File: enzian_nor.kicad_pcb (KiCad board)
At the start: 4 copper layers, 75 x 60 mm, 27 parts, among them IC1 L7809ABD2T-TR, J1 ASP-134488-01, U1 MT35XU02GCBA1G12-0AUT

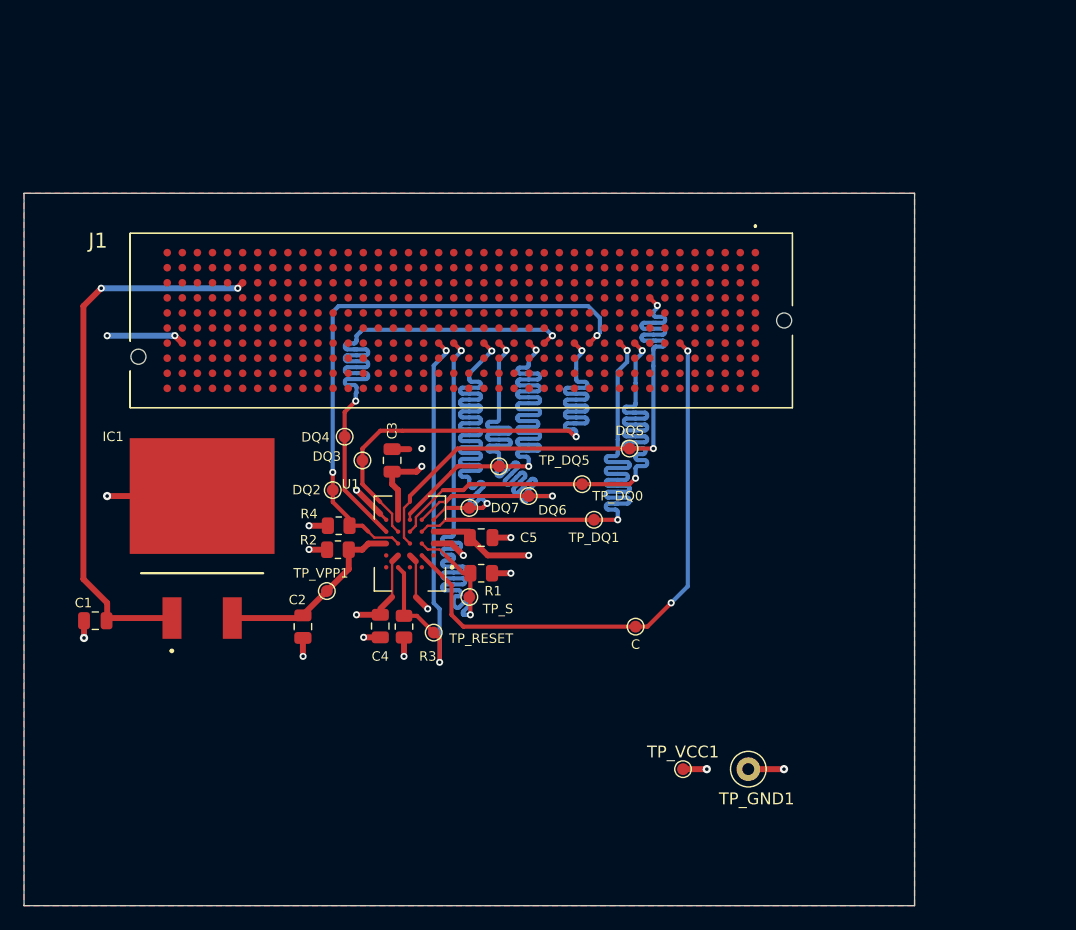
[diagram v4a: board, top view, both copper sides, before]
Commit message: Via stitching for the coplanar ground plane
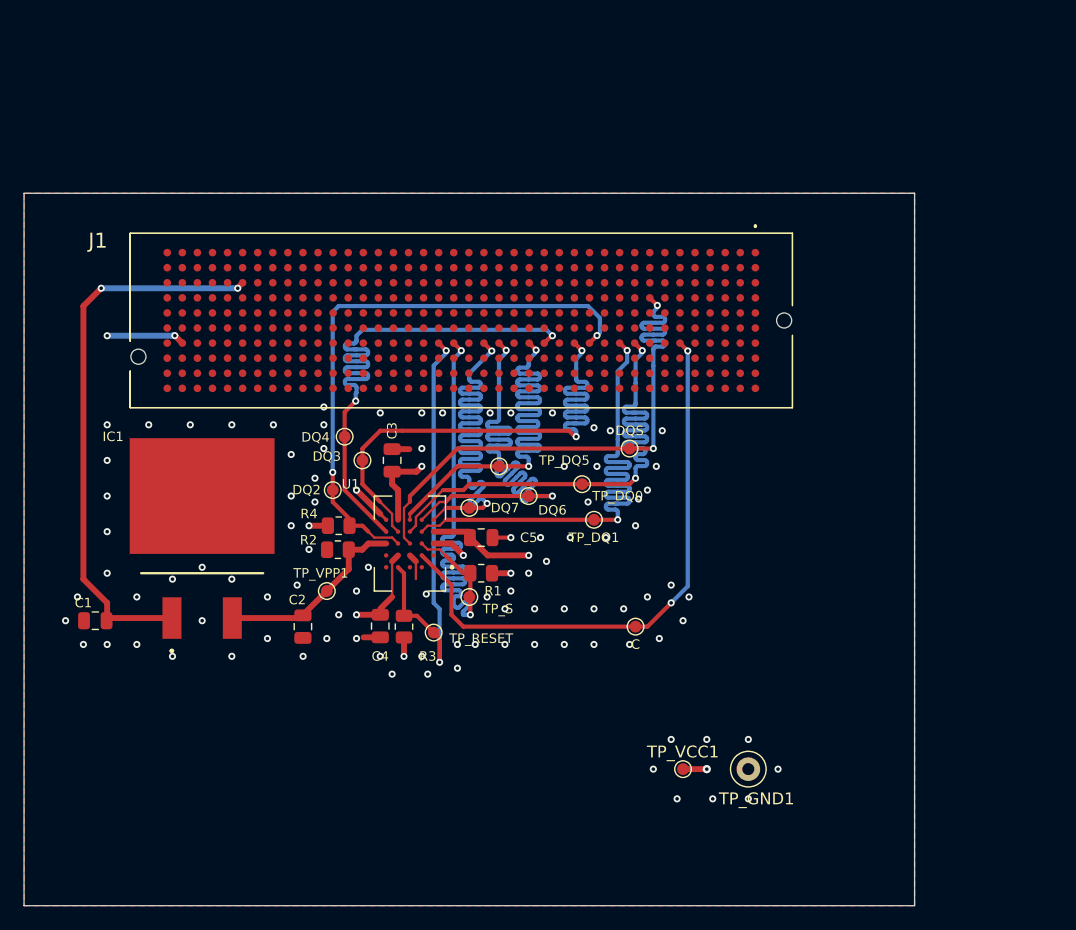
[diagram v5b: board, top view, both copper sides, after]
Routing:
- net GND: track 31.6 -> 13.2 mm, vias 11 -> 97

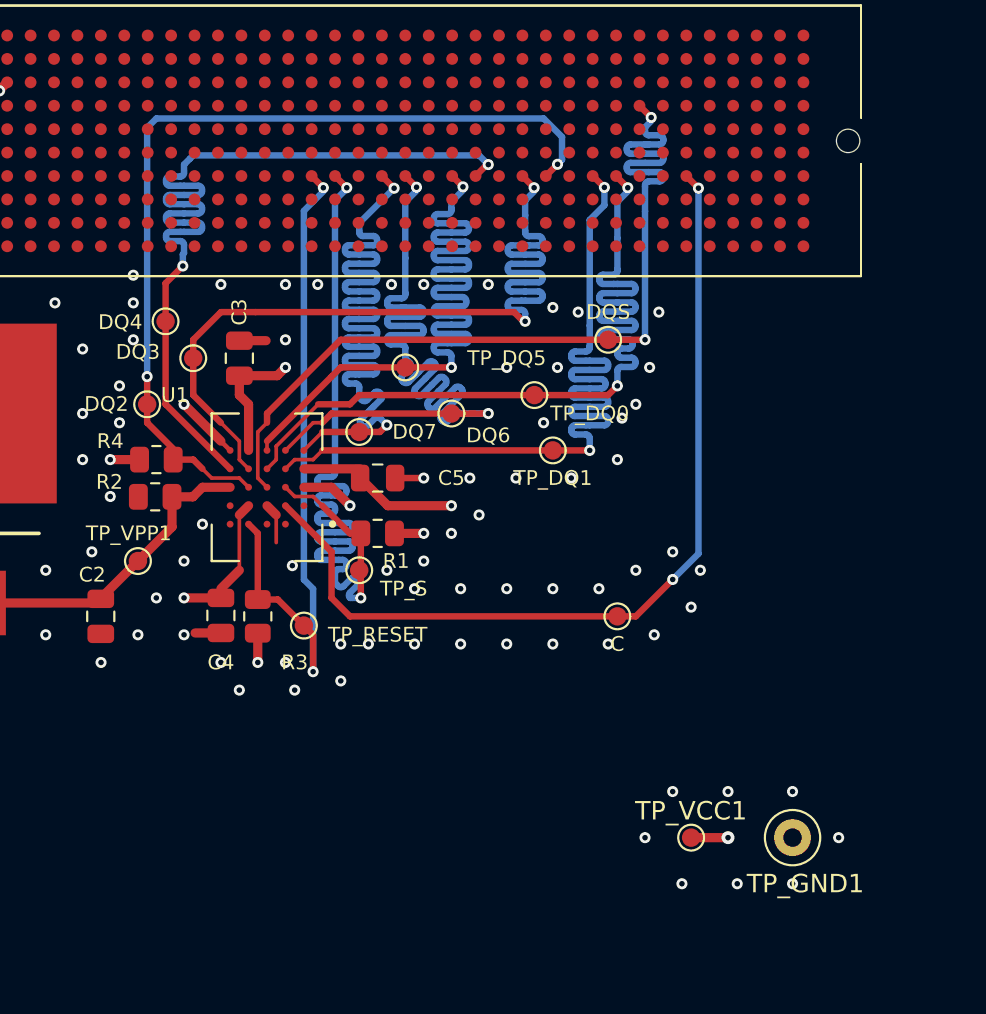
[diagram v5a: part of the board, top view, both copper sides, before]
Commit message: Revised length matching so meanders have 2x trace width between traces
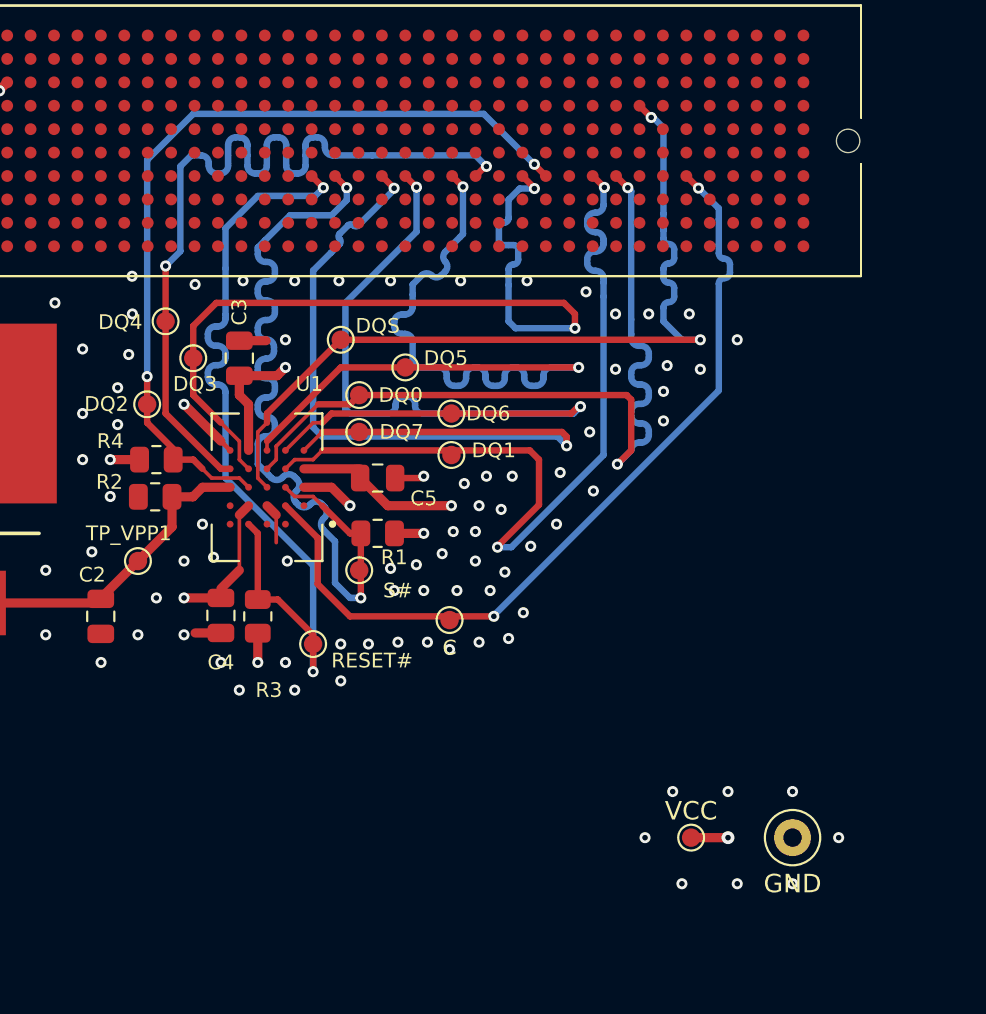
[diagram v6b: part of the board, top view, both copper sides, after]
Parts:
- moved DQS 14.5 mm to (52.5, 101.0)
- moved DQ0 9.50 mm to (53.5, 104.0)
- moved C 9.10 mm to (58.4, 116.2)
- moved DQ1 5.51 mm to (58.5, 107.2)
- moved RESET# 1.12 mm to (51.0, 117.5)
- renumbered TP_DQ0 to DQ0, TP_DQ1 to DQ1, TP_DQ5 to DQ5, TP_GND1 to GND, TP_RESET to RESET#, TP_S to S#, TP_VCC1 to VCC
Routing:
- net /NOR_RESET#: track 37.9 -> 45.5 mm
- net /NOR_S#: track 49.3 -> 45.1 mm
- net /NOR_DQ2: track 49.1 -> 45.6 mm
- net /NOR_DQ3: track 48.8 -> 45.5 mm
- net /NOR_DQ4: track 48.5 -> 45.4 mm
- net /NOR_DQ5: track 48.3 -> 45.3 mm
- net /NOR_C: track 48.5 -> 45.6 mm
- net /NOR_DQ0: track 48.3 -> 45.4 mm
- net /NOR_DQ1: track 48.4 -> 45.5 mm
- net /NOR_DQ6: track 48.3 -> 45.5 mm
- net /NOR_DQS: track 48.4 -> 45.7 mm
- net /NOR_DQ7: track 48.2 -> 45.6 mm
- net GND: vias 97 -> 104

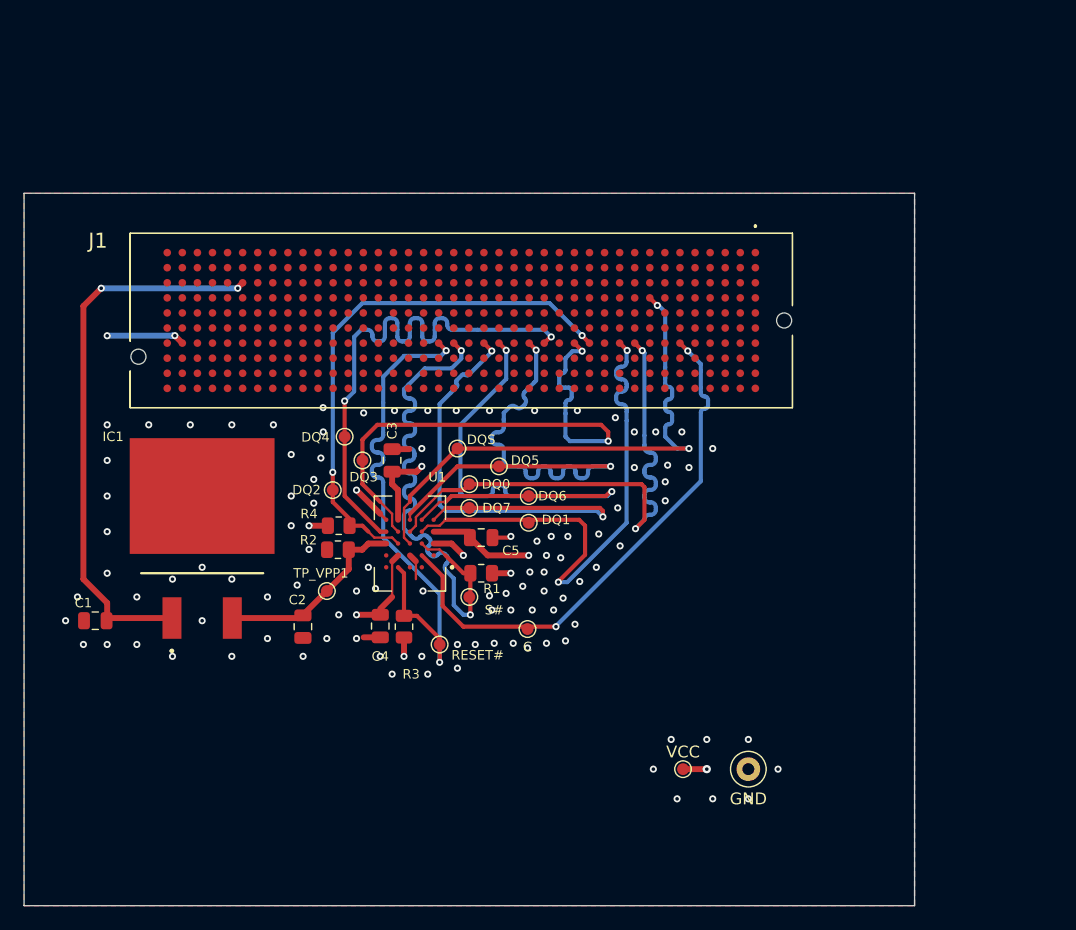
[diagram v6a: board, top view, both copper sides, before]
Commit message: Add version number, mounting holes, and minor changes to via placement
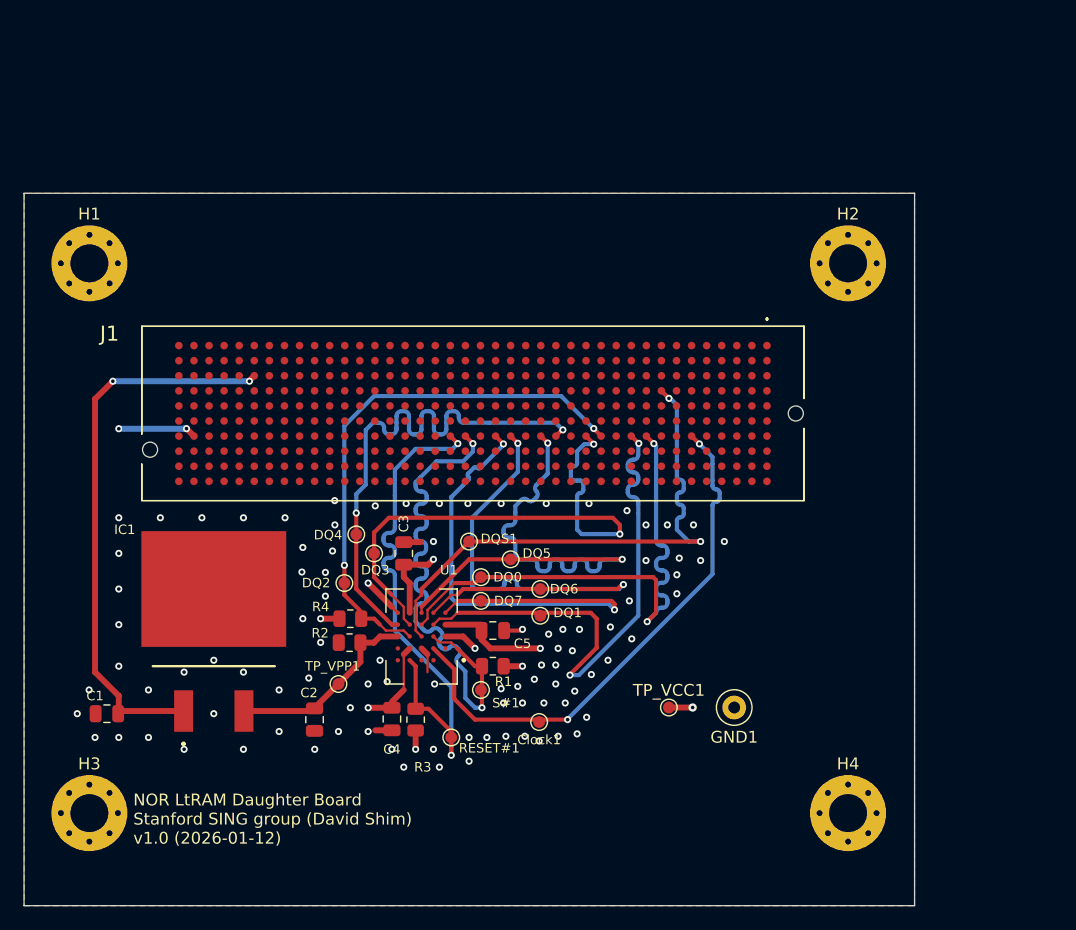
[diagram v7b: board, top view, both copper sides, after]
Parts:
- added H1: MountingHole_Pad, MountingHole:MountingHole_3.2mm_M3_Pad_Via, F.Cu at (21.5, 85.4)
- added H2: MountingHole_Pad, MountingHole:MountingHole_3.2mm_M3_Pad_Via, F.Cu at (85.4, 85.4)
- added H3: MountingHole_Pad, MountingHole:MountingHole_3.2mm_M3_Pad_Via, F.Cu at (21.5, 131.7)
- added H4: MountingHole_Pad, MountingHole:MountingHole_3.2mm_M3_Pad_Via, F.Cu at (85.4, 131.7)
- moved DQ4 8.29 mm to (44.0, 108.2)
- moved C1 7.89 mm to (23.0, 123.3)
- moved C2 7.89 mm to (40.5, 123.8)
- moved C3 7.89 mm to (48.0, 109.8)
- moved C4 7.89 mm to (47.0, 123.8)
- moved C5 7.89 mm to (55.5, 116.3)
- moved Clock1 7.89 mm to (59.4, 124.0)
- moved DQ0 7.89 mm to (54.5, 111.8)
- moved DQ1 7.89 mm to (59.5, 115.1)
- moved DQ2 7.89 mm to (43.0, 112.3)
- moved DQ3 7.89 mm to (45.5, 109.8)
- moved DQ5 7.89 mm to (57.0, 110.3)
- moved DQ6 7.89 mm to (59.5, 112.8)
- moved DQ7 7.89 mm to (54.5, 113.8)
- moved DQS1 7.89 mm to (53.5, 108.8)
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- renumbered C to Clock1, DQS to DQS1, GND to GND1, RESET# to RESET#1, S# to S#1, VCC to TP_VCC1
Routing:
- net GND: vias 104 -> 96
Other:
- board text added: "NOR LtRAM Daughter Board Stanford SING group (David Shim) v1.0 (2026-01-12)"

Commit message: Applied Mark's suggestions
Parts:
- removed C5: 100n, Capacitor_SMD:C_0805_2012Metric
- moved C4 26.1 mm to (69.5, 110.6), turned to 0 degrees
- moved C3 14.1 mm to (46.9, 123.9), turned to -90 degrees
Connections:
- J1 pad A1: unconnected-(J1-PadA1) -> GND
- J1 pad A12: unconnected-(J1-PadA12) -> GND
- J1 pad A13: unconnected-(J1-PadA13) -> GND
- J1 pad A16: unconnected-(J1-PadA16) -> GND
- J1 pad A17: unconnected-(J1-PadA17) -> GND
- J1 pad A20: unconnected-(J1-PadA20) -> GND
- J1 pad A21: unconnected-(J1-PadA21) -> GND
- J1 pad A24: unconnected-(J1-PadA24) -> GND
- J1 pad A25: unconnected-(J1-PadA25) -> GND
- J1 pad A28: unconnected-(J1-PadA28) -> GND
- J1 pad A29: unconnected-(J1-PadA29) -> GND
- J1 pad A32: unconnected-(J1-PadA32) -> GND
- J1 pad A33: unconnected-(J1-PadA33) -> GND
- J1 pad A36: unconnected-(J1-PadA36) -> GND
- J1 pad A37: unconnected-(J1-PadA37) -> GND
- J1 pad A4: unconnected-(J1-PadA4) -> GND
- J1 pad A40: unconnected-(J1-PadA40) -> GND
- J1 pad A5: unconnected-(J1-PadA5) -> GND
- J1 pad A8: unconnected-(J1-PadA8) -> GND
- J1 pad A9: unconnected-(J1-PadA9) -> GND
- J1 pad B10: unconnected-(J1-PadB10) -> GND
- J1 pad B11: unconnected-(J1-PadB11) -> GND
- J1 pad B14: unconnected-(J1-PadB14) -> GND
- J1 pad B15: unconnected-(J1-PadB15) -> GND
- J1 pad B18: unconnected-(J1-PadB18) -> GND
- J1 pad B19: unconnected-(J1-PadB19) -> GND
- J1 pad B2: unconnected-(J1-PadB2) -> GND
- J1 pad B22: unconnected-(J1-PadB22) -> GND
- J1 pad B23: unconnected-(J1-PadB23) -> GND
- J1 pad B26: unconnected-(J1-PadB26) -> GND
- J1 pad B27: unconnected-(J1-PadB27) -> GND
- J1 pad B3: unconnected-(J1-PadB3) -> GND
- J1 pad B30: unconnected-(J1-PadB30) -> GND
- J1 pad B31: unconnected-(J1-PadB31) -> GND
- J1 pad B34: unconnected-(J1-PadB34) -> GND
- J1 pad B35: unconnected-(J1-PadB35) -> GND
- J1 pad B38: unconnected-(J1-PadB38) -> GND
- J1 pad B39: unconnected-(J1-PadB39) -> GND
- J1 pad B6: unconnected-(J1-PadB6) -> GND
- J1 pad B7: unconnected-(J1-PadB7) -> GND
- J1 pad C1: unconnected-(J1-PadC1) -> GND
- J1 pad C12: unconnected-(J1-PadC12) -> GND
- J1 pad C13: unconnected-(J1-PadC13) -> GND
- J1 pad C16: unconnected-(J1-PadC16) -> GND
- J1 pad C17: unconnected-(J1-PadC17) -> GND
- J1 pad C20: unconnected-(J1-PadC20) -> GND
- J1 pad C21: unconnected-(J1-PadC21) -> GND
- J1 pad C24: unconnected-(J1-PadC24) -> GND
- J1 pad C25: unconnected-(J1-PadC25) -> GND
- J1 pad C28: unconnected-(J1-PadC28) -> GND
- J1 pad C29: unconnected-(J1-PadC29) -> GND
- J1 pad C32: unconnected-(J1-PadC32) -> GND
- J1 pad C33: unconnected-(J1-PadC33) -> GND
- J1 pad C34: unconnected-(J1-PadC34) -> GND
- J1 pad C36: unconnected-(J1-PadC36) -> GND
- J1 pad C38: unconnected-(J1-PadC38) -> GND
- J1 pad C4: unconnected-(J1-PadC4) -> GND
- J1 pad C40: unconnected-(J1-PadC40) -> GND
- J1 pad C5: unconnected-(J1-PadC5) -> GND
- J1 pad C8: unconnected-(J1-PadC8) -> GND
- J1 pad C9: unconnected-(J1-PadC9) -> GND
- J1 pad D10: unconnected-(J1-PadD10) -> GND
- J1 pad D13: unconnected-(J1-PadD13) -> GND
- J1 pad D16: unconnected-(J1-PadD16) -> GND
- J1 pad D19: unconnected-(J1-PadD19) -> GND
- J1 pad D2: unconnected-(J1-PadD2) -> GND
- J1 pad D22: unconnected-(J1-PadD22) -> GND
- J1 pad D25: unconnected-(J1-PadD25) -> GND
- J1 pad D28: unconnected-(J1-PadD28) -> GND
- J1 pad D3: unconnected-(J1-PadD3) -> GND
- J1 pad D35: unconnected-(J1-PadD35) -> GND
- J1 pad D37: unconnected-(J1-PadD37) -> GND
- J1 pad D39: unconnected-(J1-PadD39) -> GND
- J1 pad D6: unconnected-(J1-PadD6) -> GND
- J1 pad D7: unconnected-(J1-PadD7) -> GND
- J1 pad E1: unconnected-(J1-PadE1) -> GND
- J1 pad E11: unconnected-(J1-PadE11) -> GND
- J1 pad E14: unconnected-(J1-PadE14) -> GND
- J1 pad E17: unconnected-(J1-PadE17) -> GND
- J1 pad E20: unconnected-(J1-PadE20) -> GND
- J1 pad E23: unconnected-(J1-PadE23) -> GND
- J1 pad E26: unconnected-(J1-PadE26) -> GND
- J1 pad E29: unconnected-(J1-PadE29) -> GND
- J1 pad E32: unconnected-(J1-PadE32) -> GND
- J1 pad E35: unconnected-(J1-PadE35) -> GND
- J1 pad E38: unconnected-(J1-PadE38) -> GND
- J1 pad E4: unconnected-(J1-PadE4) -> GND
- J1 pad E40: unconnected-(J1-PadE40) -> GND
- J1 pad E5: unconnected-(J1-PadE5) -> GND
- J1 pad E8: unconnected-(J1-PadE8) -> GND
- J1 pad F12: unconnected-(J1-PadF12) -> GND
- J1 pad F15: unconnected-(J1-PadF15) -> GND
- J1 pad F18: unconnected-(J1-PadF18) -> GND
- J1 pad F2: unconnected-(J1-PadF2) -> GND
- J1 pad F21: unconnected-(J1-PadF21) -> GND
- J1 pad F24: unconnected-(J1-PadF24) -> GND
- J1 pad F27: unconnected-(J1-PadF27) -> GND
- J1 pad F3: unconnected-(J1-PadF3) -> GND
- J1 pad F30: unconnected-(J1-PadF30) -> GND
- J1 pad F33: unconnected-(J1-PadF33) -> GND
- J1 pad F36: unconnected-(J1-PadF36) -> GND
- J1 pad F39: unconnected-(J1-PadF39) -> GND
- J1 pad F6: unconnected-(J1-PadF6) -> GND
- J1 pad F9: unconnected-(J1-PadF9) -> GND
- J1 pad G1: unconnected-(J1-PadG1) -> GND
- J1 pad G11: unconnected-(J1-PadG11) -> GND
- J1 pad G14: unconnected-(J1-PadG14) -> GND
- J1 pad G17: unconnected-(J1-PadG17) -> GND
- J1 pad G20: unconnected-(J1-PadG20) -> GND
- J1 pad G23: unconnected-(J1-PadG23) -> GND
- J1 pad G26: unconnected-(J1-PadG26) -> GND
- J1 pad G29: unconnected-(J1-PadG29) -> GND
- J1 pad G32: unconnected-(J1-PadG32) -> GND
- J1 pad G35: unconnected-(J1-PadG35) -> GND
- J1 pad G38: unconnected-(J1-PadG38) -> GND
- J1 pad G4: unconnected-(J1-PadG4) -> GND
- J1 pad G40: unconnected-(J1-PadG40) -> GND
- J1 pad G5: unconnected-(J1-PadG5) -> GND
- J1 pad G8: unconnected-(J1-PadG8) -> GND
- J1 pad H12: unconnected-(J1-PadH12) -> GND
- J1 pad H15: unconnected-(J1-PadH15) -> GND
- J1 pad H18: unconnected-(J1-PadH18) -> GND
- J1 pad H21: unconnected-(J1-PadH21) -> GND
- J1 pad H24: unconnected-(J1-PadH24) -> GND
- J1 pad H27: unconnected-(J1-PadH27) -> GND
- J1 pad H3: unconnected-(J1-PadH3) -> GND
- J1 pad H30: unconnected-(J1-PadH30) -> GND
- J1 pad H33: unconnected-(J1-PadH33) -> GND
- J1 pad H36: unconnected-(J1-PadH36) -> GND
- J1 pad H39: unconnected-(J1-PadH39) -> GND
- J1 pad H6: unconnected-(J1-PadH6) -> GND
- J1 pad H9: unconnected-(J1-PadH9) -> GND
- J1 pad J1: unconnected-(J1-PadJ1) -> GND
- J1 pad J11: unconnected-(J1-PadJ11) -> GND
- J1 pad J14: unconnected-(J1-PadJ14) -> GND
- J1 pad J17: unconnected-(J1-PadJ17) -> GND
- J1 pad J20: unconnected-(J1-PadJ20) -> GND
- J1 pad J23: unconnected-(J1-PadJ23) -> GND
- J1 pad J26: unconnected-(J1-PadJ26) -> GND
- J1 pad J29: unconnected-(J1-PadJ29) -> GND
- J1 pad J32: unconnected-(J1-PadJ32) -> GND
- J1 pad J35: unconnected-(J1-PadJ35) -> GND
- J1 pad J38: unconnected-(J1-PadJ38) -> GND
- J1 pad J4: unconnected-(J1-PadJ4) -> GND
- J1 pad J40: unconnected-(J1-PadJ40) -> GND
- J1 pad J5: unconnected-(J1-PadJ5) -> GND
- J1 pad J8: unconnected-(J1-PadJ8) -> GND
- J1 pad K12: unconnected-(J1-PadK12) -> GND
- J1 pad K15: unconnected-(J1-PadK15) -> GND
- J1 pad K18: unconnected-(J1-PadK18) -> GND
- J1 pad K2: unconnected-(J1-PadK2) -> GND
- J1 pad K21: unconnected-(J1-PadK21) -> GND
- J1 pad K24: unconnected-(J1-PadK24) -> GND
- J1 pad K27: unconnected-(J1-PadK27) -> GND
- J1 pad K3: unconnected-(J1-PadK3) -> GND
- J1 pad K30: unconnected-(J1-PadK30) -> GND
- J1 pad K33: unconnected-(J1-PadK33) -> GND
- J1 pad K36: unconnected-(J1-PadK36) -> GND
- J1 pad K39: unconnected-(J1-PadK39) -> GND
- J1 pad K6: unconnected-(J1-PadK6) -> GND
- J1 pad K9: unconnected-(J1-PadK9) -> GND
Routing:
- net GND: track 13.2 -> 133.2 mm, vias 96 -> 251
- net VCC: track 37.0 -> 16.5 mm, vias 9 -> 11
